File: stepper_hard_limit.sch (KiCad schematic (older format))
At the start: 19 parts, among them J1 PWR, J2 SW1, J3 SW2, J4 DRIVER_MOTOR, J5 CONTROL, U1 4093

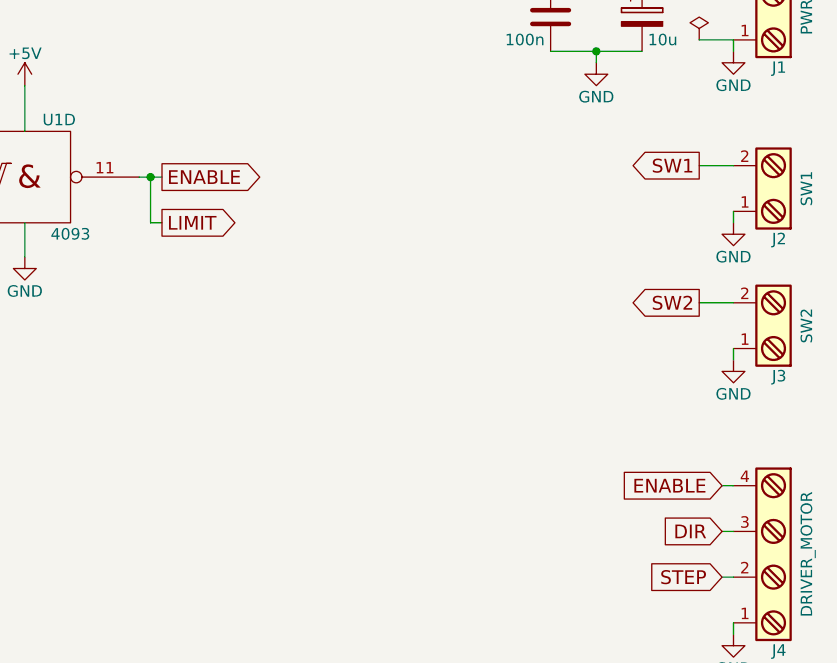
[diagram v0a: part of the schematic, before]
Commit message: ENABLE is active low
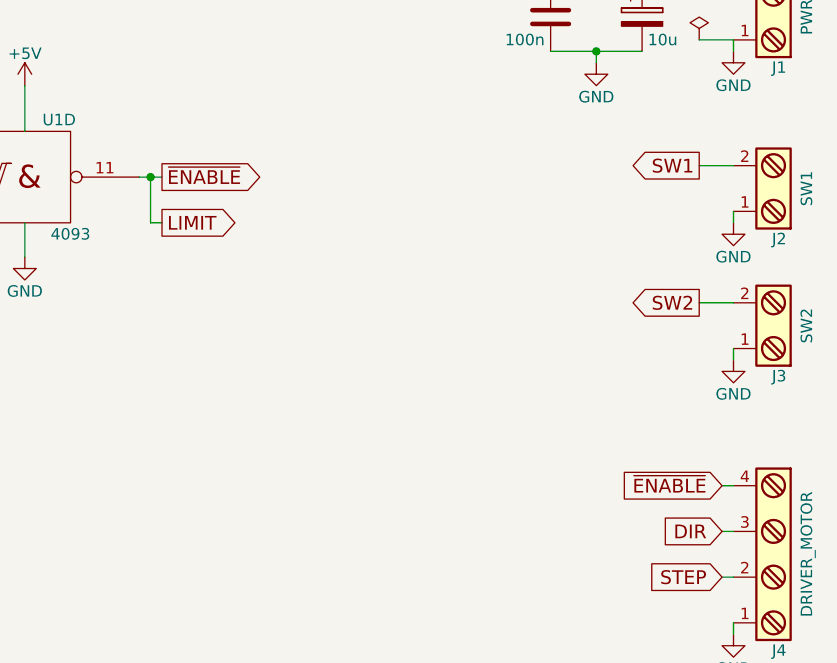
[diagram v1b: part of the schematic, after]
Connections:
- net ENABLE renamed LIMIT
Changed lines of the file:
@@
 Connection ~ 2750 3050
 Text GLabel 5350 2250 2    60   Output ~ 0
-ENABLE
+~ENABLE
 $Comp
 L C C1
@@
 DIR
 Text GLabel 7800 3600 0    60   Input ~ 0
-ENABLE
+~ENABLE
 Wire Wire Line
 	7800 3600 7850 3600
